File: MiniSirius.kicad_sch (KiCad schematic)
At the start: 51 parts, among them J1 Conn_Coaxial_SMA, J2 Molex_MCRF_73412-0110, J3 JST_03, SW1 Slide_Switch_SPDT, U1 RFM95W-868S2, U2 MAX-M10S, U3 L7805

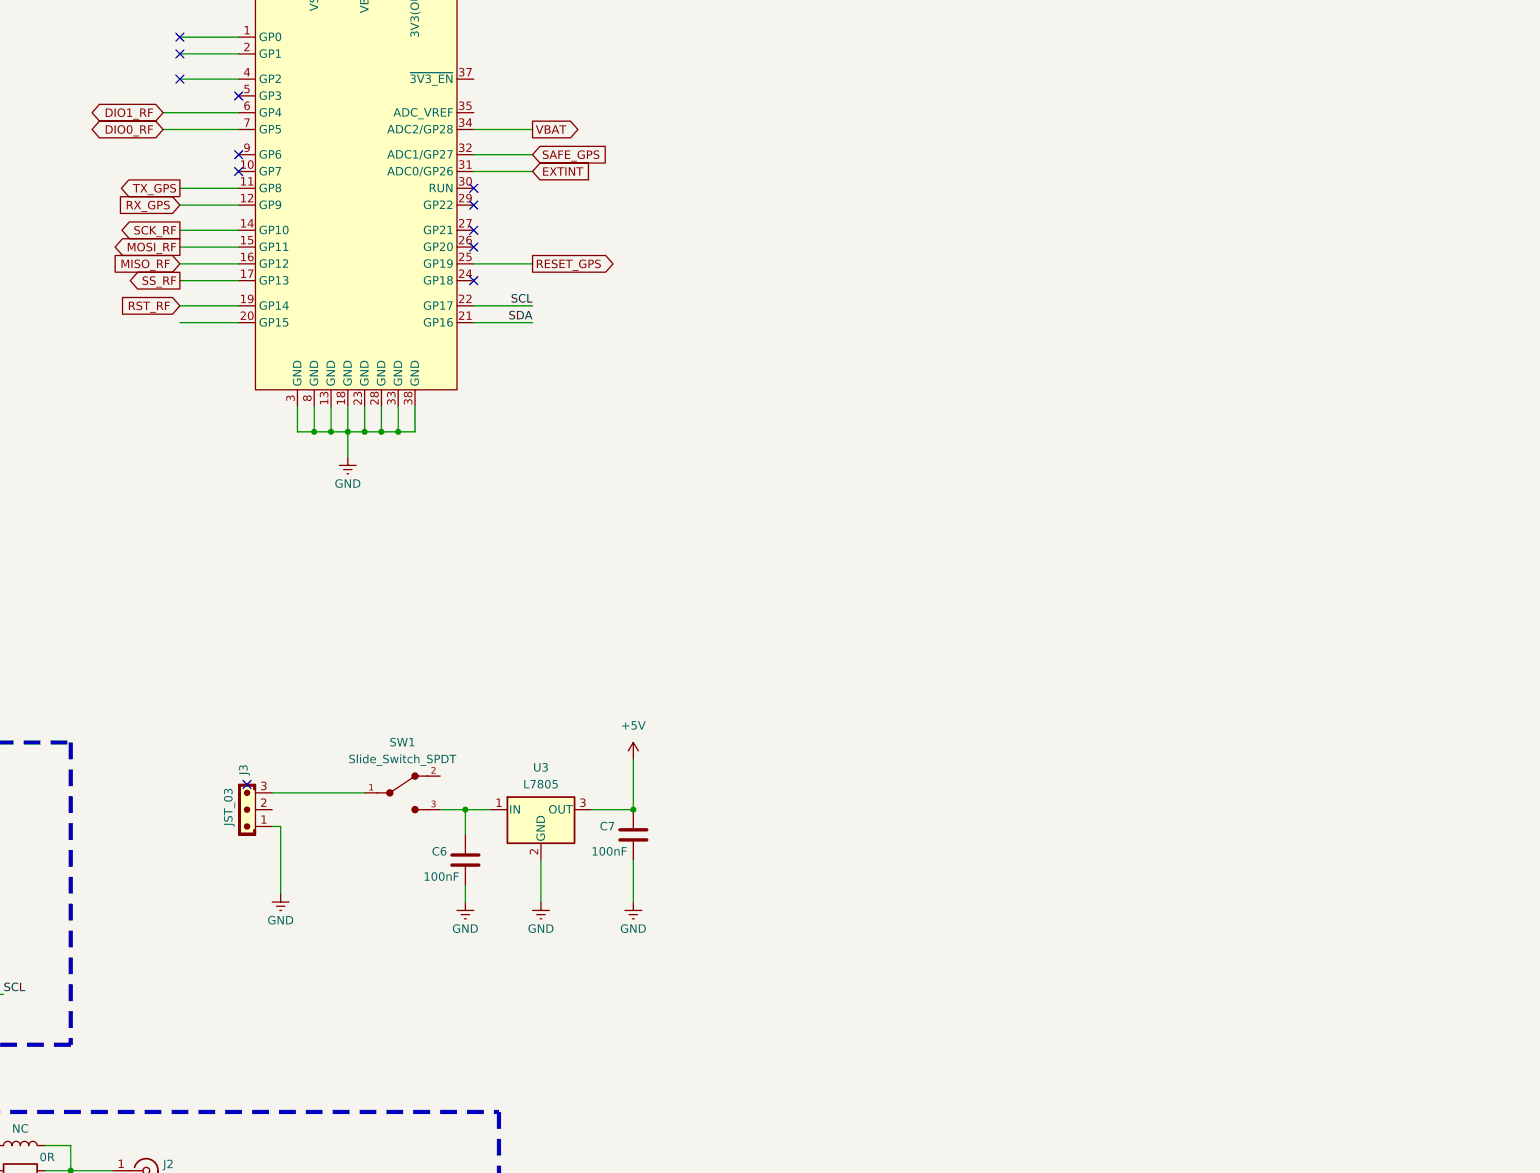
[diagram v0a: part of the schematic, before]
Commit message: update schematic
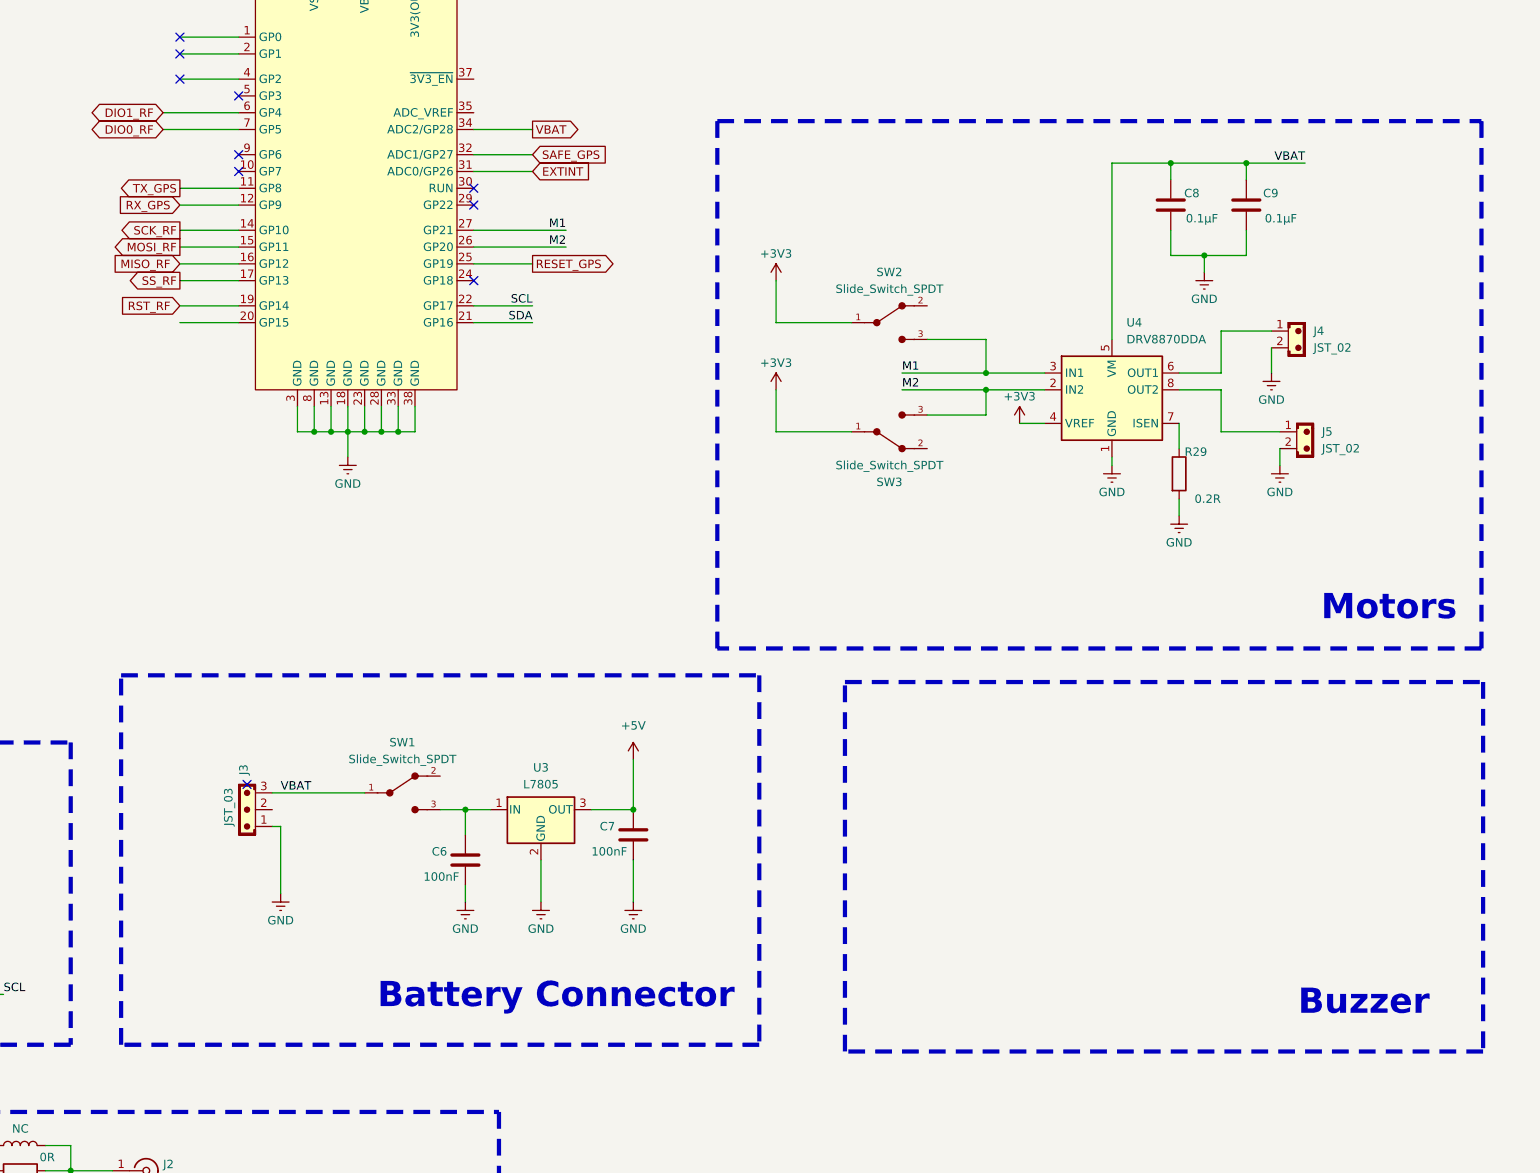
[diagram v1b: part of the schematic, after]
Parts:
- added C8, C9: 0.1µF, symbol Device:C
- added J4, J5: JST_02, Connector_JST:JST_EH_B2B-EH-A_1x02_P2.50mm_Vertical, symbol PCM_SL_Connectors:JST_02
- added R29: 0.2R, Resistor_SMD:R_0201_0603Metric, symbol Device:R
- added SW2, SW3: Slide_Switch_SPDT, PCM_SL_Devices:Slide_Switch_SPDT_P3mm_10x5x10mm, symbol PCM_SL_Devices:Slide_Switch_SPDT_P3mm_10x5x10mm
- added U4: DRV8870DDA, Package_SO:Texas_HTSOP-8-1EP_3.9x4.9mm_P1.27mm_EP2.95x4.9mm_Mask2.4x3.1mm_ThermalVias, symbol Driver_Motor:DRV8870DDA
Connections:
- net +3V3: now also SW2.1, SW3.1, U4.4 (VREF)
- net GND: now also C8.2, C9.2, J4.2, J5.2, R29.2, U4.1 (GND), U4.9 (GND)
- net VBAT: now also J3.3, SW1.1, C8.1, C9.1, U4.5 (VM)
- net M2: now reaches A1.26 (GP20)
- net M2: now also SW3.3, U4.2 (IN2)
- net M1: now reaches A1.27 (GP21)
- net M1: now also SW2.3, U4.3 (IN1)
- new net: J4.1, U4.6 (OUT1)
- new net: R29.1, U4.7 (ISEN)
- new net: J5.1, U4.8 (OUT2)
- no-connect marks 19 -> 17
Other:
- note added: "Battery Connector"
- note added: "Buzzer"
- note added: "Motors"

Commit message: Update Schematic with buzzer, IMU and motor control + schematic pdf export
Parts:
- removed SW2, SW3: Slide_Switch_SPDT, PCM_SL_Devices:Slide_Switch_SPDT_P3mm_10x5x10mm, symbol PCM_SL_Devices:Slide_Switch_SPDT_P3mm_10x5x10mm
- added BZ1: Buzzer, Buzzer_Beeper:Buzzer_CUI_CPT-9019S-SMT, symbol Device:Buzzer
- added C10, C11: 100nF, symbol Device:C
- added D2: 1N4148WT, Diode_SMD:D_SOD-523, symbol Diode:1N4148WT
- added J2: JST_03, Connector_JST:JST_EH_B3B-EH-A_1x03_P2.50mm_Vertical, symbol PCM_SL_Connectors:JST_03
- added J4: JST_04, Connector_JST:JST_EH_S4B-EH_1x04_P2.50mm_Horizontal, symbol PCM_SL_Connectors:JST_04
- added Q1: BSS138, Package_TO_SOT_SMD:SOT-23, symbol Transistor_FET:BSS138
- added R19, R2, R32: 10k, Resistor_SMD:R_0201_0603Metric, symbol Device:R
- added SW1, SW2: Push_Button, Button_Switch_THT:SW_PUSH_6mm, symbol PCM_SL_Devices:Push_Button
- added U6: LSM6DSL, Package_LGA:LGA-14_3x2.5mm_P0.5mm_LayoutBorder3x4y, symbol Sensor_Motion:LSM6DSL
- renumbered J2 to J5, J3 to J6, J4 to J7, J5 to J8, R9 to R10, R10 to R11, R11 to R12, R12 to R13, R13 to R14, R14 to R15, R15 to R16, R16 to R17, R17 to R18, R18 to R20, R19 to R21, R20 to R22, R21 to R23, R22 to R24, R23 to R25, R24 to R26, R25 to R27, R26 to R28, R27 to R29, R2 to R3, R28 to R30, R29 to R31, R3 to R4, R4 to R5, R5 to R6, R6 to R7, R7 to R8, R8 to R9, SW1 to SW3, U3 to U4, U4 to U5
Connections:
- net +3V3: now also C10.1, C11.1, J2.2, J4.3, R19.2, R2.2, U6.12 (CS), U6.5 (VDDIO), U6.8 (VDD)
- net GND: now also C10.2, C11.2, J2.3, J4.4, Q1.2 (S), R32.1, SW1.2, SW2.2, U6.1 (SDO/SA0), U6.2 (SDX), U6.3 (SCX), U6.6 (GND), U6.7 (GND)
- net SCL: now also J4.2, U6.13 (SCL)
- net SDA: now also J4.1, U6.14 (SDA)
- net VBAT: now also BZ1.1 (+), D2.1 (K)
- net INT1_IMU: now reaches A1.1 (GP0)
- net INT1_IMU: now also U6.4 (INT1)
- net M2_Button: now reaches A1.10 (GP7)
- net M2_Button: now also R19.1, SW2.1
- net INT2_IMU: now reaches A1.2 (GP1)
- net INT2_IMU: now also U6.9 (INT2)
- net M1_Button: now reaches A1.9 (GP6)
- net M1_Button: now also R2.1, SW1.1
- new net: BZ1.2 (-), D2.2 (A), Q1.3 (D)
- new net BUZZER_PIN: Q1.1 (G), R32.2
- new net PWM_1: J2.1
- no-connect marks 17 -> 9
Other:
- note added: "External connectors"
- note added: "IMU"
- note added: "Motors Controler"
- moved on the sheet: A1, C6, C7, H1, H2, H3, H4, J6, R27, R28, SW3, U4

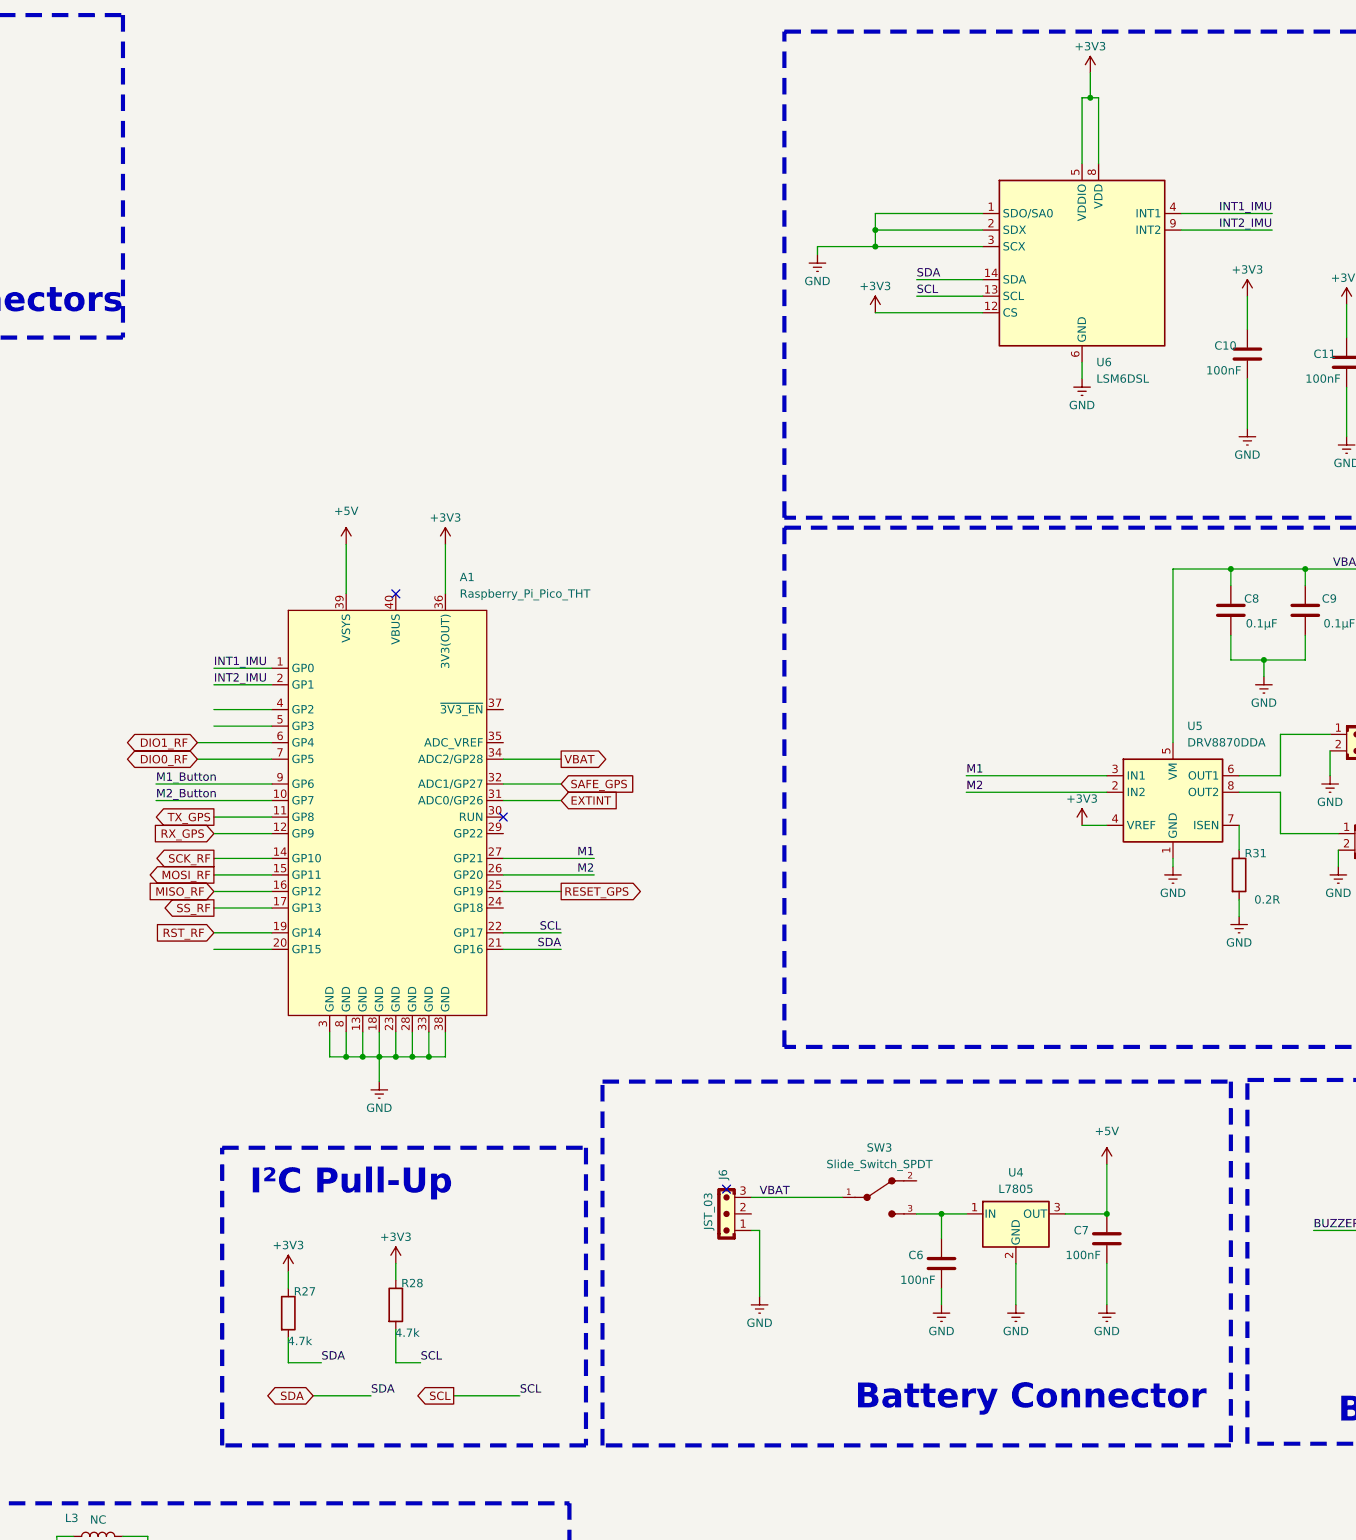
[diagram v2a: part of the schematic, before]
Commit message: Update Schematic with buzzer, IMU and motor control + schematic pdf export
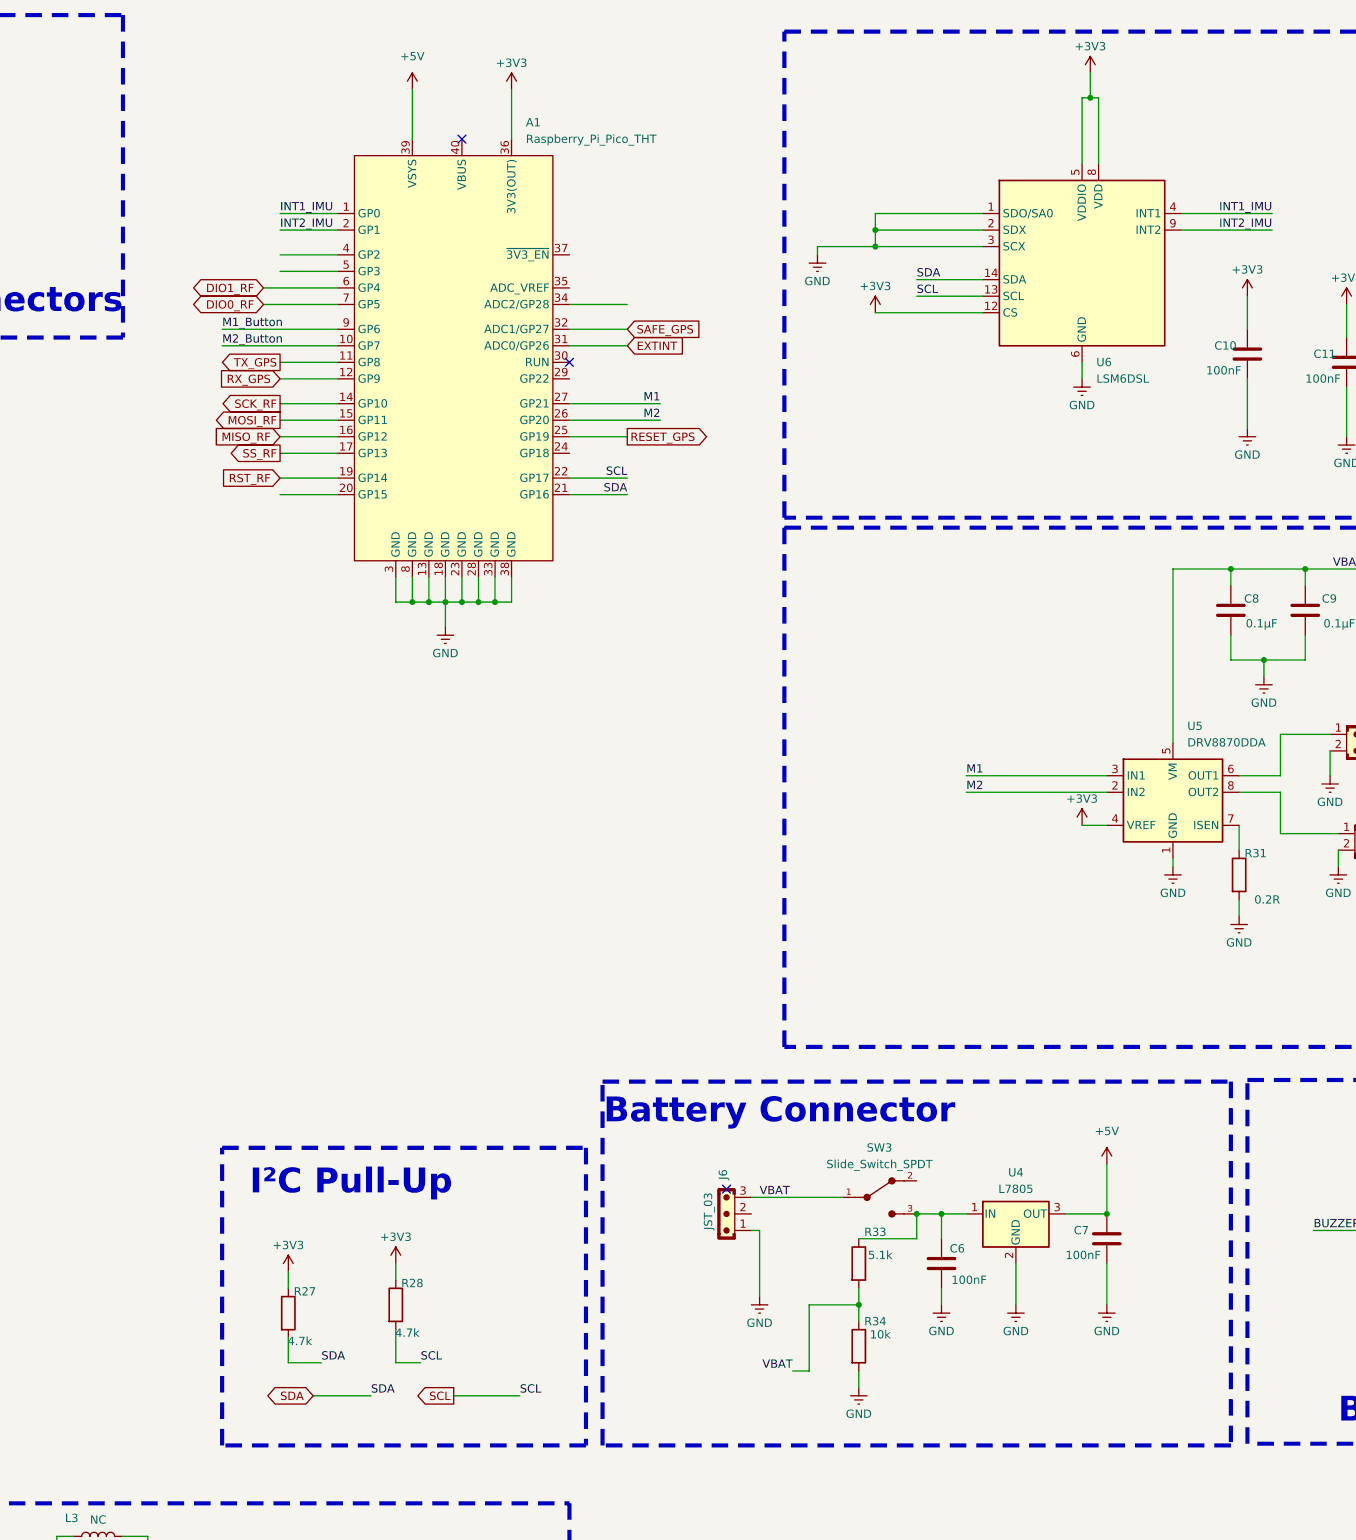
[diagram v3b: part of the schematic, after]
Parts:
- added R33: 5.1k, Resistor_SMD:R_0603_1608Metric_Pad0.98x0.95mm_HandSolder, symbol Device:R
- added R34: 10k, Resistor_SMD:R_0603_1608Metric_Pad0.98x0.95mm_HandSolder, symbol Device:R
- C1, C2, C3, C4, C5: footprint Capacitor_SMD:C_0402_1005Metric -> Capacitor_SMD:C_0603_1608Metric_Pad1.08x0.95mm_HandSolder
- C10, C11, C6, C7, C8, C9: footprint (none) -> Capacitor_SMD:C_0603_1608Metric_Pad1.08x0.95mm_HandSolder
- L1, L2, L3: footprint Inductor_SMD:L_0603_1608Metric -> Inductor_SMD:L_0603_1608Metric_Pad1.05x0.95mm_HandSolder
- R1, R10, R11, R12, R13, R14, R15, R16, R17, R18, R19, R2, R20, R21, R22, R23, R24, R25, R26, R27, R28, R29, R3, R30, R31, R32, R4, R5, R6, R7, R8, R9: footprint Resistor_SMD:R_0201_0603Metric -> Resistor_SMD:R_0603_1608Metric_Pad0.98x0.95mm_HandSolder
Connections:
- net GND: now also R34.2
- net VBAT: now also R33.2, R34.1; no longer A1.34 (ADC2/GP28)
- net at C6.1, SW3.3, U4.1 (IN): now also R33.1
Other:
- moved on the sheet: A1
